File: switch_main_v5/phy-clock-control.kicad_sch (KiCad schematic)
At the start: 42 parts, among them Q1101 DMN21D2UFB-7B, Q1102 DMN21D2UFB-7B, Q1103 DMN21D2UFB-7B, U1101 LMK1C1104DQFR, U1102 LMK1C1104DQFR, U1103 NX3L4051HRZ

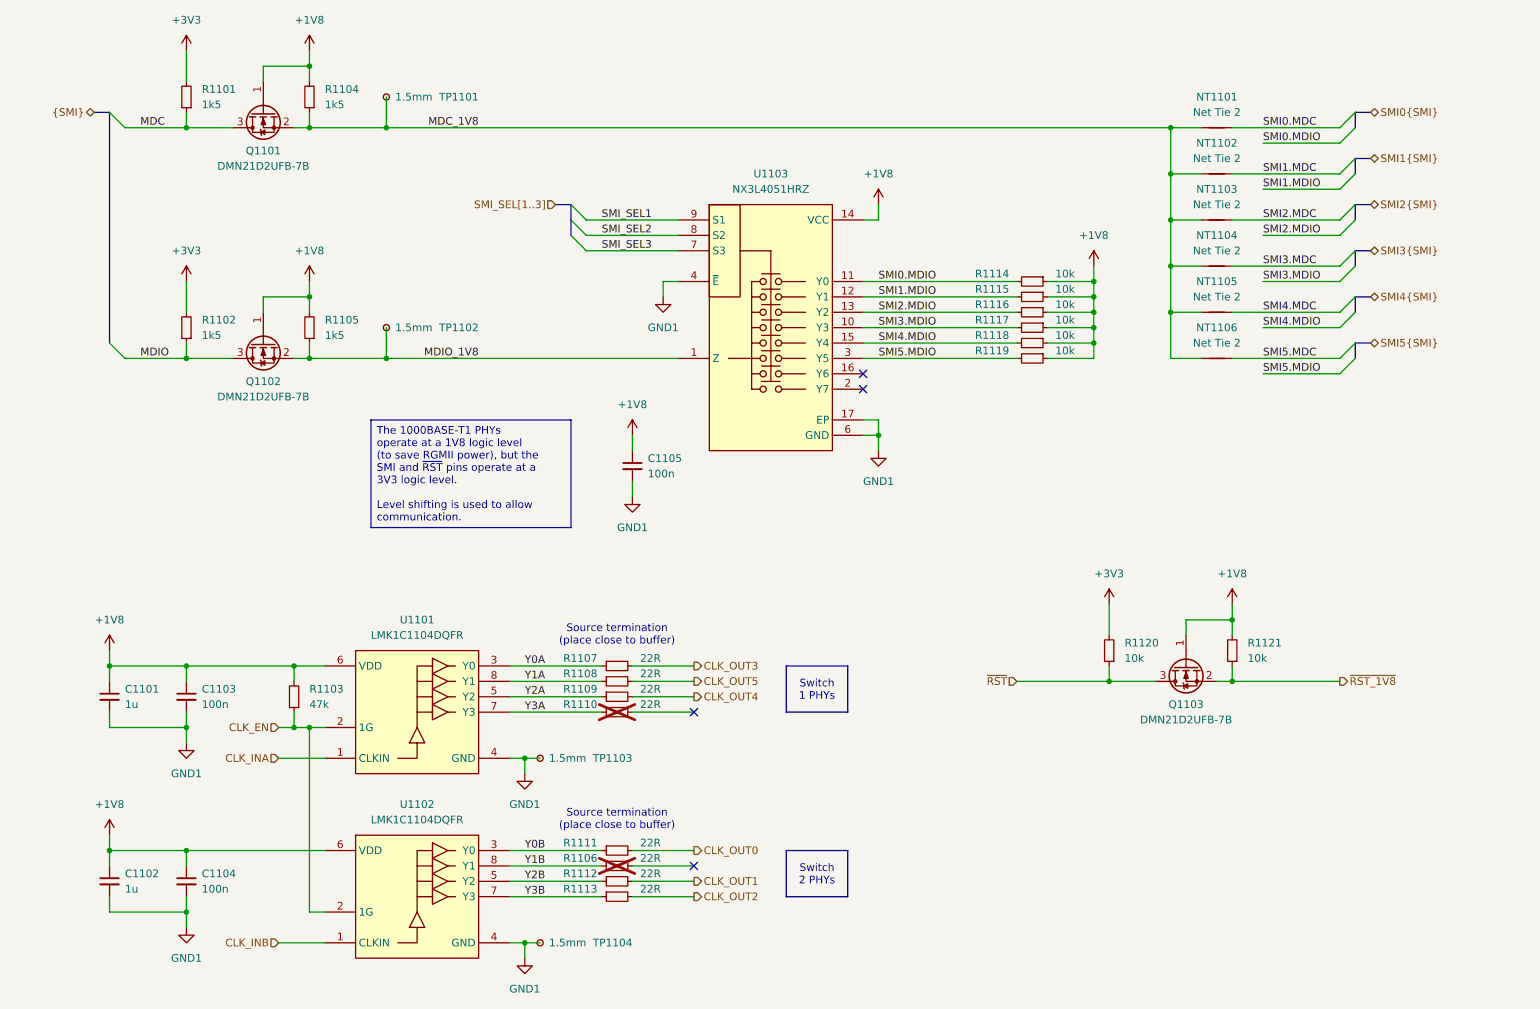
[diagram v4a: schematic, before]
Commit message: Fixed test points
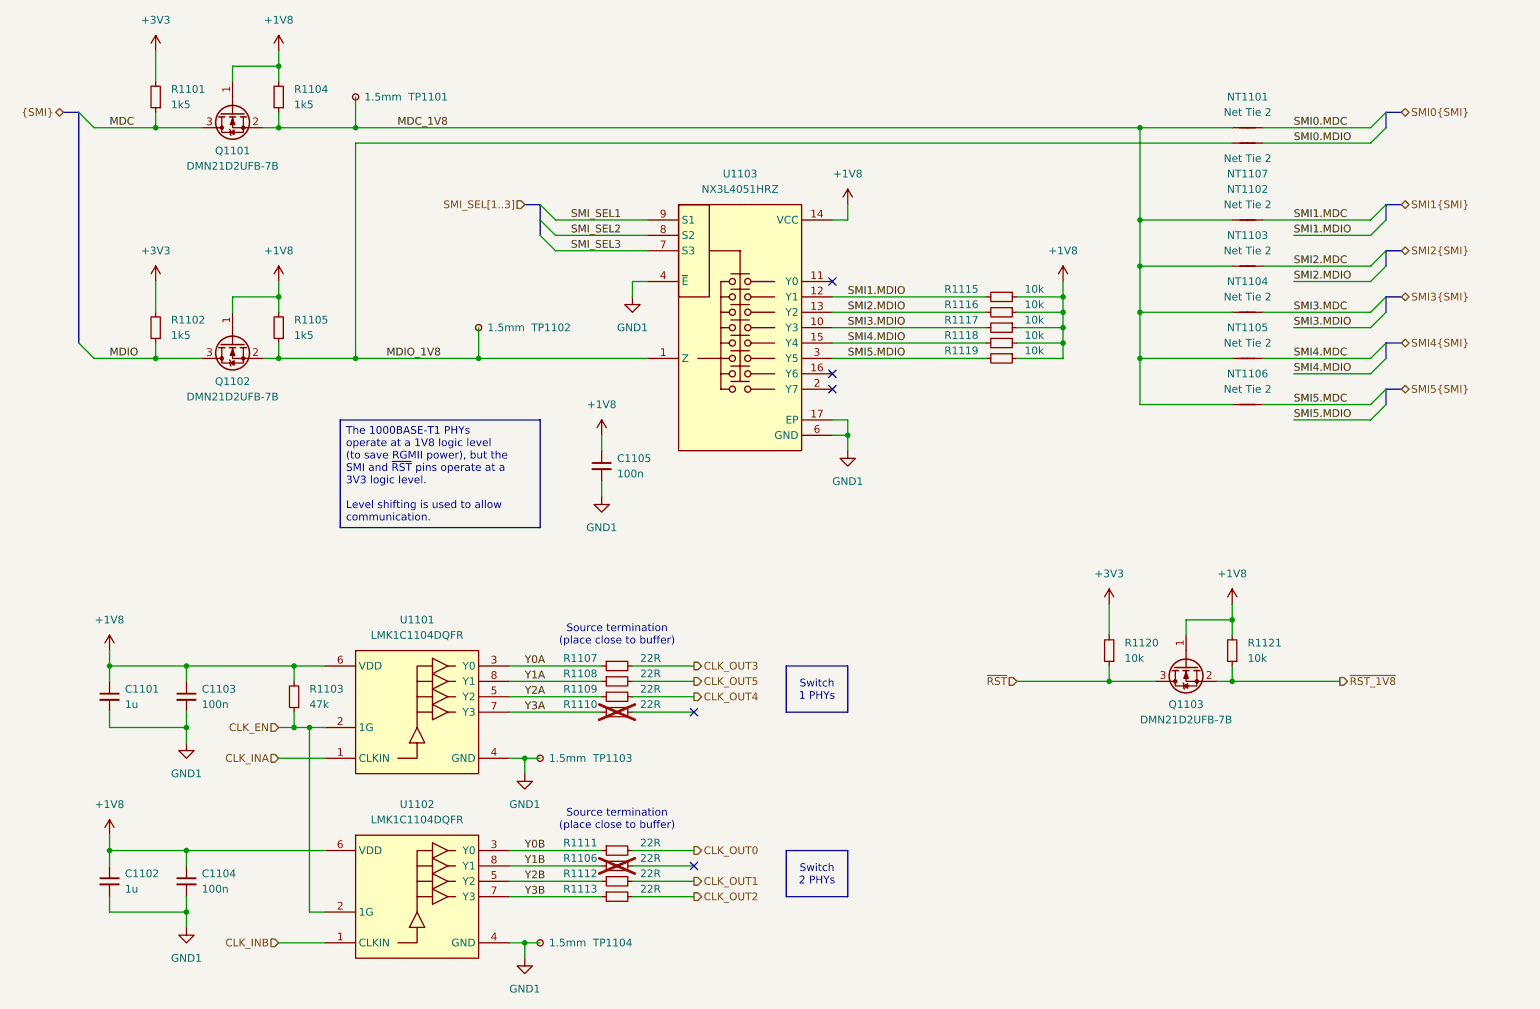
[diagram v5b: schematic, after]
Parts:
- removed R1114: 10k, Resistor_SMD:R_0402_1005Metric, symbol Device:R_Small
- added NT1107: Net Tie 2, project_footprints:NetTie-2_SMD_Pad0.15mm, symbol NET-TIE:NetTie_2
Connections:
- net MDIO_1V8: now also NT1107.1
- net SMI0.MDIO: now also NT1107.2; no longer U1103.11 (Y0)
- no-connect marks 4 -> 5
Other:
- moved on the sheet: C1105, NT1101, NT1102, NT1103, NT1104, NT1105, NT1106, Q1101, Q1102, R1101, R1102, R1104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

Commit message: Moved 0V9 regulators
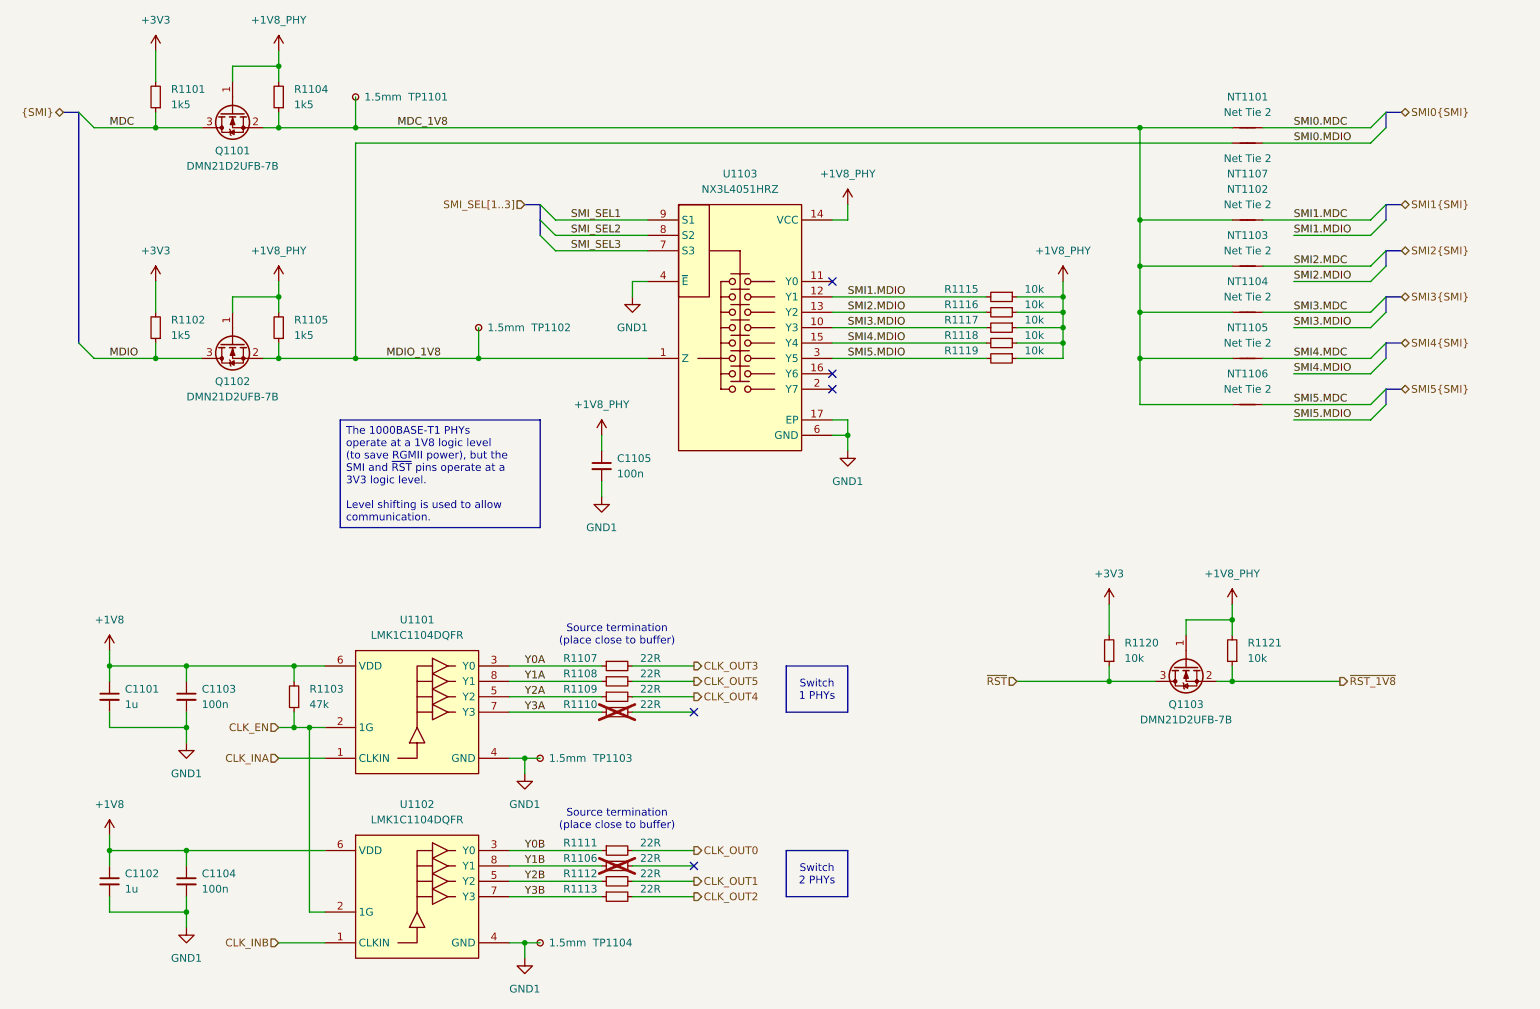
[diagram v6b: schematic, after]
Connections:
- net +1V8: no longer C1105.1, Q1101.1 (G), Q1102.1 (G), Q1103.1 (G), R1104.2, R1105.2, R1115.1, R1116.1, R1117.1, R1118.1, R1119.1, R1121.2, U1103.14 (VCC)
- new net +1V8_PHY: C1105.1, Q1101.1 (G), Q1102.1 (G), Q1103.1 (G), R1104.2, R1105.2, R1115.1, R1116.1, R1117.1, R1118.1, R1119.1, R1121.2, U1103.14 (VCC)

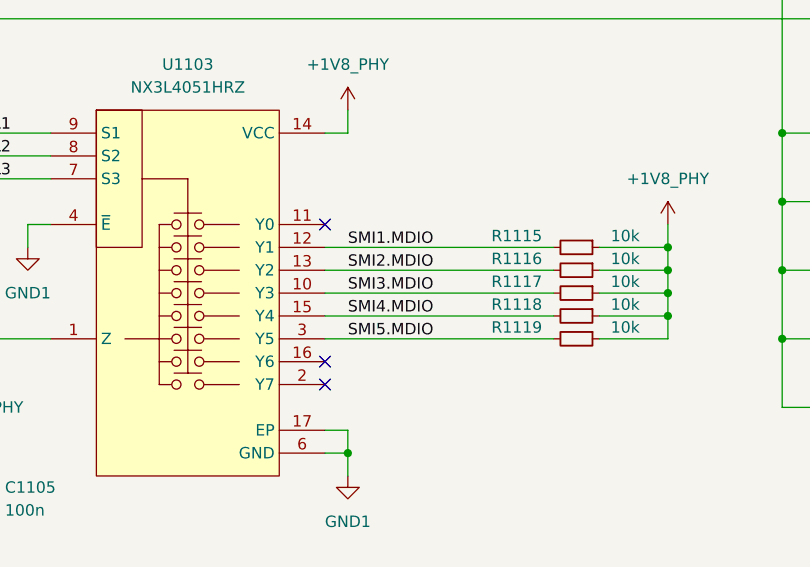
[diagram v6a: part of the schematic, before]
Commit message: All signals routed, need to do power still
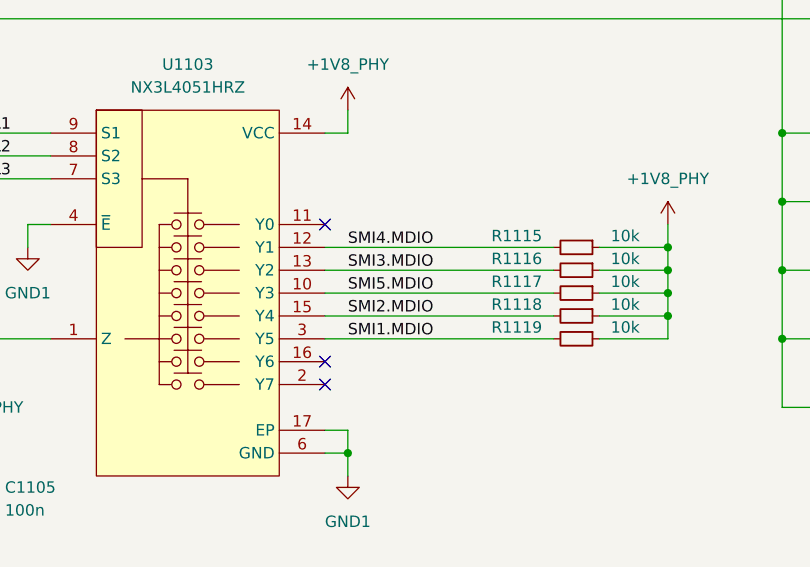
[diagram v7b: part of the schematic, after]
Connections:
- net SMI1.MDIO: now also R1119.2, U1103.3 (Y5); no longer R1115.2, U1103.12 (Y1)
- net SMI2.MDIO: now also R1118.2, U1103.15 (Y4); no longer R1116.2, U1103.13 (Y2)
- net SMI3.MDIO: now also R1116.2, U1103.13 (Y2); no longer R1117.2, U1103.10 (Y3)
- net SMI4.MDIO: now also R1115.2, U1103.12 (Y1); no longer R1118.2, U1103.15 (Y4)
- net SMI5.MDIO: now also R1117.2, U1103.10 (Y3); no longer R1119.2, U1103.3 (Y5)
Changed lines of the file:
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@@
 	)
 	(label "SMI4.MDIO"
-		(at 165.1 76.2 0)
+		(at 165.1 68.58 0)
 		(effects
 			(font
@@
 	)
 	(label "SMI3.MDIO"
-		(at 165.1 73.66 0)
+		(at 165.1 71.12 0)
 		(effects
 			(font
@@
 	)
 	(label "SMI1.MDIO"
-		(at 165.1 68.58 0)
+		(at 165.1 78.74 0)
 		(effects
 			(font
@@
 	)
 	(label "SMI5.MDIO"
-		(at 165.1 78.74 0)
+		(at 165.1 73.66 0)
 		(effects
 			(font
@@
 	)
 	(label "SMI2.MDIO"
-		(at 165.1 71.12 0)
-		(effects
-			(font
+		(at 165.1 76.2 0)
+		(effects
+			(font

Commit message: Tidied schematic and PCB
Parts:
- R1803: renamed from R1115; value 10k -> 22k
- R1804: renamed from R1116; value 10k -> 22k
- R1807: renamed from R1117; value 10k -> 22k
- R1808: renamed from R1118; value 10k -> 22k
- R1809: renamed from R1119; value 10k -> 22k
- renumbered C1105 to C1801, C1101 to C1802, C1103 to C1803, C1102 to C1804, C1104 to C1805, NT1101 to NT1801, NT1107 to NT1802, NT1102 to NT1803, NT1103 to NT1804, NT1104 to NT1805, NT1105 to NT1806, NT1106 to NT1807, Q1101 to Q1801, Q1102 to Q1802, Q1103 to Q1803, R1101 to R1801, R1104 to R1802, R1102 to R1805, R1105 to R1806, R1107 to R1810, R1108 to R1811, R1103 to R1812, R1109 to R1813, R1110 to R1814, R1120 to R1815, R1121 to R1816, R1111 to R1817, R1106 to R1818, R1112 to R1819, R1113 to R1820, TP1101 to TP1801, TP1102 to TP1802, TP1103 to TP1803, TP1104 to TP1804, U1103 to U1801, U1101 to U1802, U1102 to U1803
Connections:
- net +1V8_PHY: no longer R1803.1, R1804.1, R1807.1, R1808.1, R1809.1
- net GND1: now also R1803.1, R1804.1, R1807.1, R1808.1, R1809.1
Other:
- moved on the sheet: Q1803, R1815, R1816
